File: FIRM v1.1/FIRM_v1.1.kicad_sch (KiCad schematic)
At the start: 107 parts, among them J1 Pin, J2 Conn_01x02_Pin, J3 FIRM2 Conn, U1 W25N01KVZEIR, U11 SCH16T-K01-10, U12 STM32F446ZCH6, U2 ADXL375, U3 TPS2121RUXR, U4 ICM45686, U5 INA219AxDCN, U7 BMP581, U8 MMC5983MA, U9 A-USBC-20F0-EA-GSR05, Y1 12 MHz

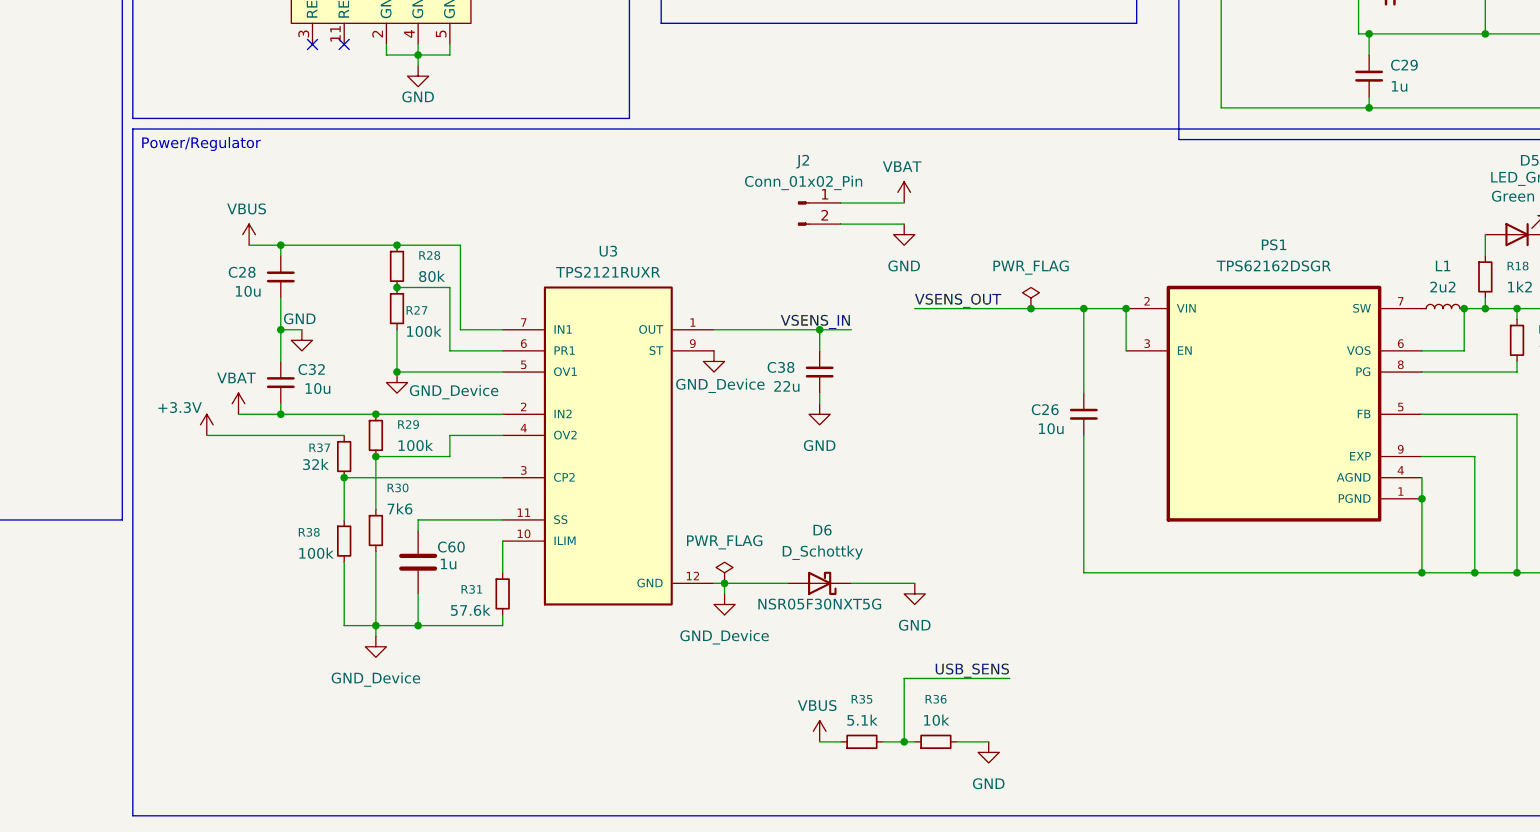
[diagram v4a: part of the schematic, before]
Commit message: Added a Pfet for polirization detection
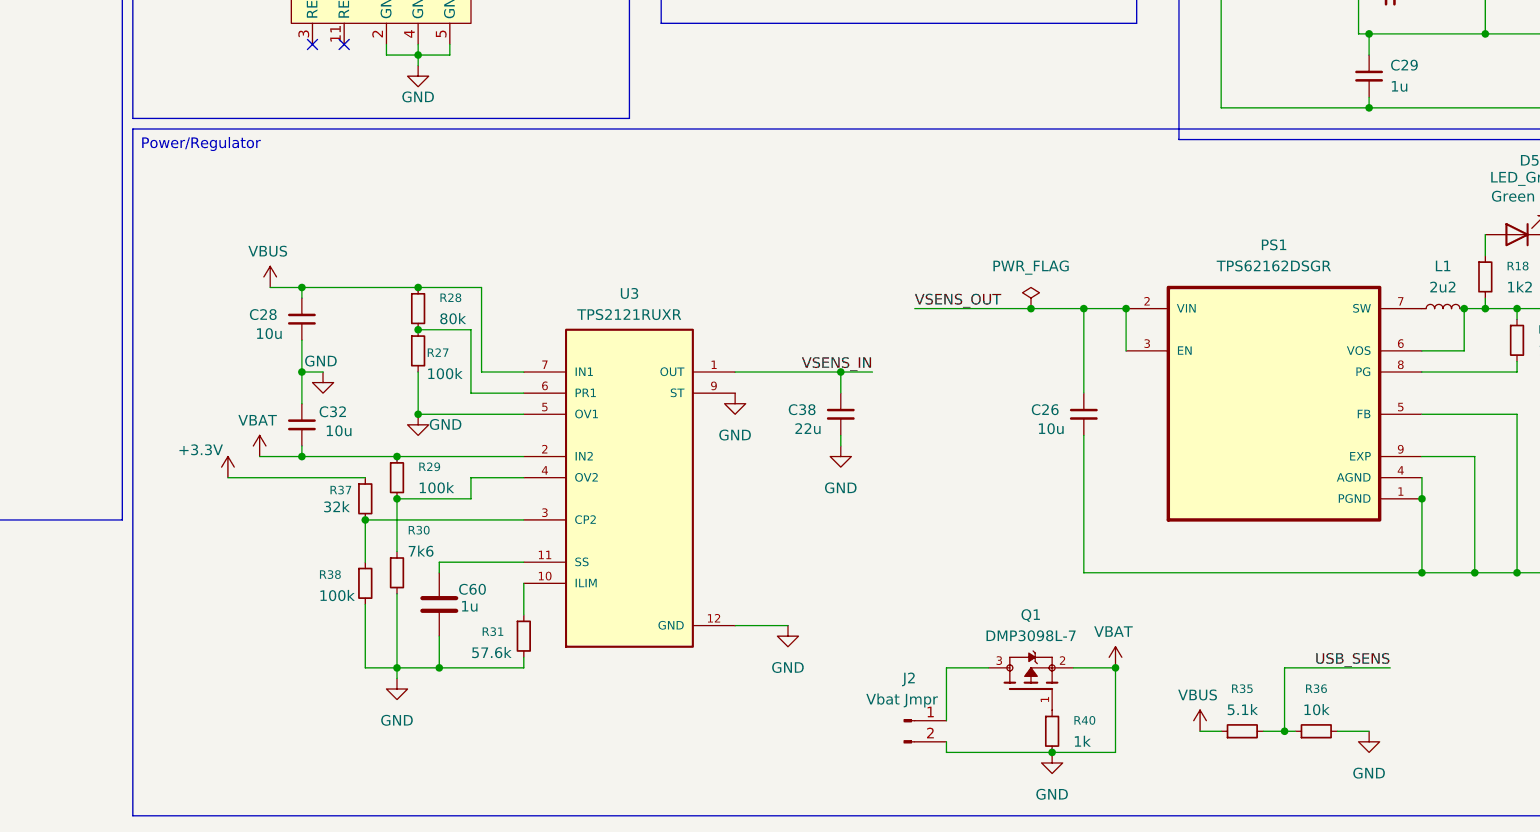
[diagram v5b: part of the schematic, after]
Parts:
- removed D6: D_Schottky, HPRC_Connectors:D_schottky_NSR05F30NXT5G, symbol Device:D_Schottky
- added Q1: DMP3098L-7, HPRC_Logic:DMP3098L-7, symbol HPRC_Logic_ICs:DMP3098L-7
- added R40: 1k, Resistor_SMD:R_0402_1005Metric, symbol Device:R_Small
- J2: value Conn_01x02_Pin -> Vbat Jmpr
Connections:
- net GND_Device is gone; now on net GND: C60.2, R27.2, R30.2, R31.2, R38.2, U3.12 (GND), U3.5 (OV1), U3.9 (ST)
- net GND: now also C32.2, R29.1, U3.2 (IN2), U3.2_1 (IN2), Q1.2, R40.2
- removed net VBAT: C32.2, J2.1 (Pin_1), R29.1, U3.2 (IN2), U3.2_1 (IN2)
- new net: J2.1 (Pin_1), Q1.3
- new net: Q1.1, R40.1
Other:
- moved on the sheet: C28, C32, C38, C60, J2, R27, R28, R29, R30, R31, R35, R36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

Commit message: Changed C38 and C26 to X7R caps
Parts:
- C26: footprint Capacitor_SMD:C_0603_1608Metric -> Capacitor_SMD:C_1206_3216Metric; Digikey PN 490-12737-1-ND -> 490-6518-1-ND; MPN GRM188R61E106MA73J -> GRM31CR71E106KA12L
- C38: footprint Capacitor_SMD:C_0805_2012Metric -> Capacitor_SMD:C_1210_3225Metric; Digikey PN 4713-GMC21X5R226M25NTCT-ND -> 490-GRM32ER71E226KE15KCT-ND; MPN GMC21X5R226M25NT -> GRM32ER71E226KE15K
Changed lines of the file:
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@@
 			)
 		)
-		(property "Footprint" "Capacitor_SMD:C_0603_1608Metric"
+		(property "Footprint" "Capacitor_SMD:C_1206_3216Metric"
 			(at 429.26 238.76 0)
 			(hide yes)
@@
 			)
 		)
-		(property "Datasheet" ""
+		(property "Datasheet" "https://mm.digikey.com/Volume0/opasdata/d220001/medias/docus/8942/490_Chip_Multilayer_CAT2021_MLCC.pdf"
 			(at 429.26 238.76 0)
 			(hide yes)
@@
 			)
 		)
-		(property "Description" "Unpolarized capacitor, small symbol"
+		(property "Description" "X7R Unpolarized capacitor."
 			(at 429.26 238.76 0)
 			(hide yes)
@@
 			)
 		)
-		(property "MPN" "GRM188R61E106MA73J"
+		(property "MPN" "GRM31CR71E106KA12L"
 			(at 429.26 238.76 0)
 			(hide yes)
@@
 			)
 		)
-		(property "Digikey PN" "490-12737-1-ND"
+		(property "Digikey PN" "490-6518-1-ND"
 			(at 429.26 238.76 0)
 			(hide yes)
@@
 			)
 		)
-		(property "Footprint" "Capacitor_SMD:C_0805_2012Metric"
+		(property "Footprint" "Capacitor_SMD:C_1210_3225Metric"
 			(at 400.05 238.76 0)
 			(hide yes)
@@
 			)
 		)
-		(property "Datasheet" ""
+		(property "Datasheet" "https://mm.digikey.com/Volume0/opasdata/d220001/medias/docus/8942/490_Chip_Multilayer_CAT2021_MLCC.pdf"
 			(at 400.05 238.76 0)
 			(hide yes)
@@
 			)
 		)
-		(property "Description" "Unpolarized capacitor, small symbol"
+		(property "Description" "X7R Unpolarized capacitor."
 			(at 400.05 238.76 0)
 			(hide yes)
@@
 			)
 		)
-		(property "MPN" "GMC21X5R226M25NT"
+		(property "MPN" "GRM32ER71E226KE15K"
 			(at 400.05 238.76 0)
 			(hide yes)
@@
 			)
 		)
-		(property "Digikey PN" "4713-GMC21X5R226M25NTCT-ND"
+		(property "Digikey PN" "490-GRM32ER71E226KE15KCT-ND"
 			(at 400.05 238.76 0)
 			(hide yes)

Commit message: Changed missmatched footprints
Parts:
- C12, C34, C39, C40, C41, C42, C43, C45, C48, C52, C54, C55, C58, C7, C8, C9: footprint Capacitor_SMD:C_0402_1005Metric -> Capacitor_SMD:C_0201_0603Metric
- J1: footprint Connector_PinHeader_1.00mm:PinHeader_1x06_P1.00mm_Vertical -> Connector_PinHeader_2.54mm:PinHeader_1x06_P2.54mm_Vertical
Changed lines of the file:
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@@
 			)
 		)
-		(property "Footprint" "Capacitor_SMD:C_0402_1005Metric"
+		(property "Footprint" "Capacitor_SMD:C_0201_0603Metric"
 			(at 126.6952 73.66 0)
 			(hide yes)
@@
 			)
 		)
-		(property "Footprint" "Capacitor_SMD:C_0402_1005Metric"
+		(property "Footprint" "Capacitor_SMD:C_0201_0603Metric"
 			(at 144.4752 52.07 0)
 			(hide yes)
@@
 			)
 		)
-		(property "Footprint" "Capacitor_SMD:C_0402_1005Metric"
+		(property "Footprint" "Capacitor_SMD:C_0201_0603Metric"
 			(at 97.4852 52.07 0)
 			(hide yes)
@@
 			)
 		)
-		(property "Footprint" "Capacitor_SMD:C_0402_1005Metric"
+		(property "Footprint" "Capacitor_SMD:C_0201_0603Metric"
 			(at 108.9152 52.07 0)
 			(hide yes)
@@
 			)
 		)
-		(property "Footprint" "Capacitor_SMD:C_0402_1005Metric"
+		(property "Footprint" "Capacitor_SMD:C_0201_0603Metric"
 			(at 120.3452 52.07 0)
 			(hide yes)
@@
 			)
 		)
-		(property "Footprint" "Capacitor_SMD:C_0402_1005Metric"
+		(property "Footprint" "Capacitor_SMD:C_0201_0603Metric"
 			(at 167.3352 52.07 0)
 			(hide yes)
@@
 			)
 		)
-		(property "Footprint" "Capacitor_SMD:C_0402_1005Metric"
+		(property "Footprint" "Capacitor_SMD:C_0201_0603Metric"
 			(at 178.7652 52.07 0)
 			(hide yes)
@@
 			)
 		)
-		(property "Footprint" "Capacitor_SMD:C_0402_1005Metric"
+		(property "Footprint" "Capacitor_SMD:C_0201_0603Metric"
 			(at 155.9052 52.07 0)
 			(hide yes)
@@
 			)
 		)
-		(property "Footprint" "Capacitor_SMD:C_0402_1005Metric"
+		(property "Footprint" "Capacitor_SMD:C_0201_0603Metric"
 			(at 133.0452 52.07 0)
 			(hide yes)
@@
 			)
 		)
-		(property "Footprint" "Capacitor_SMD:C_0402_1005Metric"
+		(property "Footprint" "Capacitor_SMD:C_0201_0603Metric"
 			(at 39.0652 52.07 0)
 			(hide yes)
@@
 			)
 		)
-		(property "Footprint" "Capacitor_SMD:C_0402_1005Metric"
+		(property "Footprint" "Capacitor_SMD:C_0201_0603Metric"
 			(at 136.8552 81.28 0)
 			(hide yes)
@@
 			)
 		)
-		(property "Footprint" "Capacitor_SMD:C_0402_1005Metric"
+		(property "Footprint" "Capacitor_SMD:C_0201_0603Metric"
 			(at 27.6352 52.07 0)
 			(hide yes)
@@
 			)
 		)
-		(property "Footprint" "Connector_PinHeader_1.00mm:PinHeader_1x06_P1.00mm_Vertical"
+		(property "Footprint" "Connector_PinHeader_2.54mm:PinHeader_1x06_P2.54mm_Vertical"
 			(at 354.33 34.29 0)
 			(hide yes)
@@
 			)
 		)
-		(property "Footprint" "Capacitor_SMD:C_0402_1005Metric"
+		(property "Footprint" "Capacitor_SMD:C_0201_0603Metric"
 			(at 50.4952 52.07 0)
 			(hide yes)
@@
 			)
 		)
-		(property "Footprint" "Capacitor_SMD:C_0402_1005Metric"
+		(property "Footprint" "Capacitor_SMD:C_0201_0603Metric"
 			(at 86.0552 52.07 0)
 			(hide yes)
@@
 			)
 		)
-		(property "Footprint" "Capacitor_SMD:C_0402_1005Metric"
+		(property "Footprint" "Capacitor_SMD:C_0201_0603Metric"
 			(at 73.3552 52.07 0)
 			(hide yes)
@@
 			)
 		)
-		(property "Footprint" "Capacitor_SMD:C_0402_1005Metric"
+		(property "Footprint" "Capacitor_SMD:C_0201_0603Metric"
 			(at 61.9252 52.07 0)
 			(hide yes)
